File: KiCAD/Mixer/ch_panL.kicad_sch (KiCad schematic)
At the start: 8 parts, among them J4 Conn_01x02_Socket, J5 Conn_01x02_Socket, U1 NE5532

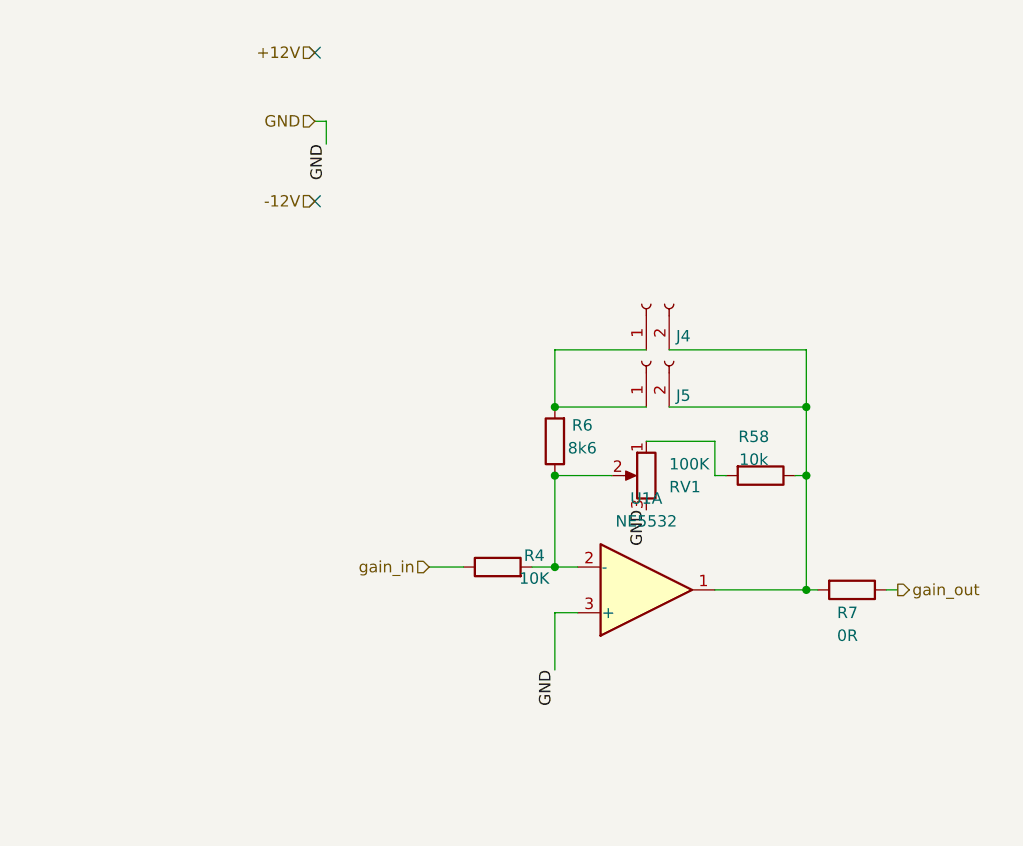
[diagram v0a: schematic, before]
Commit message: Rework of schematic, with error fixes and reworked pcb
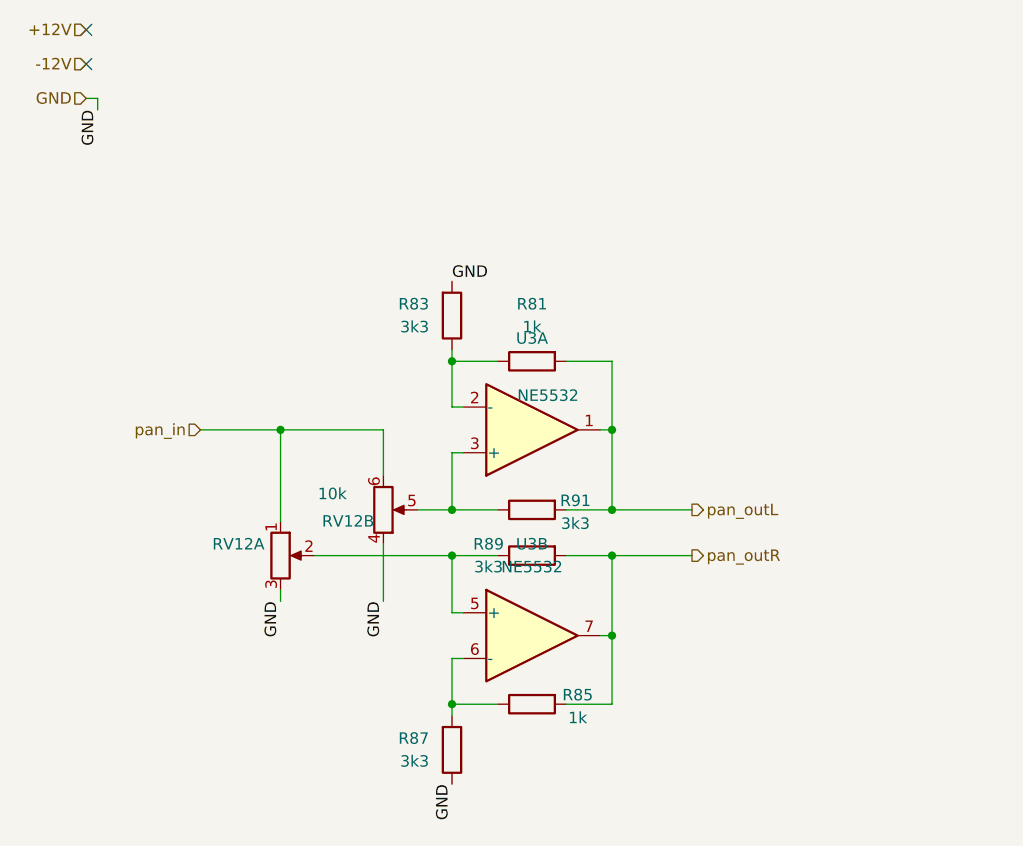
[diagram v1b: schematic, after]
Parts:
- removed J4, J5: Conn_01x02_Socket, Connector_PinSocket_2.54mm:PinSocket_1x02_P2.54mm_Vertical, symbol Connector:Conn_01x02_Socket
- removed R4: 10K, Resistor_SMD:R_0805_2012Metric_Pad1.20x1.40mm_HandSolder, symbol Device:R
- removed R58: 10k, Resistor_SMD:R_0805_2012Metric_Pad1.20x1.40mm_HandSolder, symbol Device:R
- removed R6: 8k6, Resistor_SMD:R_0805_2012Metric_Pad1.20x1.40mm_HandSolder, symbol Device:R
- removed R7: 0R, Resistor_SMD:R_0805_2012Metric_Pad1.20x1.40mm_HandSolder, symbol Device:R
- removed RV1: 100K, Potentiometer_THT:Potentiometer_Alps_RK09K_Single_Vertical, symbol Device:R_Potentiometer
- removed U1: NE5532, Package_SO:SOIC-8_3.9x4.9mm_P1.27mm, symbol Amplifier_Operational:NE5532
- added R81, R85: 1k, Resistor_SMD:R_0805_2012Metric_Pad1.20x1.40mm_HandSolder, symbol Device:R
- added R83, R87, R89, R91: 3k3, Resistor_SMD:R_0805_2012Metric_Pad1.20x1.40mm_HandSolder, symbol Device:R
- added RV12: 10k, Potentiometer_THT:Potentiometer_Alps_RK09L_Double_Vertical, symbol Device:R_Potentiometer_Dual_Separate
- added U3: NE5532, Package_SO:SOIC-8_3.9x4.9mm_P1.27mm, symbol Amplifier_Operational:NE5532
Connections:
- net GND: now also R83.2, R87.1, RV12.3, RV12.4
- new net: R89.1, RV12.2, U3.5 (+)
- new net: R81.1, R83.1, U3.2 (-)
- new net: R91.1, RV12.5, U3.3 (+)
- new net: R85.1, R87.2, U3.6 (-)
- new net pan_in: RV12.1, RV12.6
- new net pan_outL: R81.2, R91.2, U3.1
- new net pan_outR: R85.2, R89.2, U3.7

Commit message: Final PCB Version that got ordered from JLCPCB
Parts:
- removed R81, R85: 1k, Resistor_SMD:R_0805_2012Metric_Pad1.20x1.40mm_HandSolder, symbol Device:R
- removed R83, R87, R89, R91: 3k3, Resistor_SMD:R_0805_2012Metric_Pad1.20x1.40mm_HandSolder, symbol Device:R
- removed RV12: 10k, Potentiometer_THT:Potentiometer_Alps_RK09L_Double_Vertical, symbol Device:R_Potentiometer_Dual_Separate
- added R69, R70, R72, R73: 3k3, Resistor_SMD:R_0805_2012Metric_Pad1.20x1.40mm_HandSolder, symbol Device:R
- added R71, R74: 1k, Resistor_SMD:R_0805_2012Metric_Pad1.20x1.40mm_HandSolder, symbol Device:R
- added RV10: 10k, Potentiometer_THT:Potentiometer_Alps_RK09L_Double_Vertical, symbol Device:R_Potentiometer_Dual_Separate
- renumbered U3 to U10
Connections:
- net GND: now also R69.2, R70.1, RV10.3, RV10.4
- net pan_in: now also RV10.1, RV10.6
- net pan_outL: now also R71.2, R72.2
- net pan_outR: now also R73.2, R74.2
- net at U10.5 (+): now also R73.1, RV10.2
- net at U10.2 (-): now also R69.1, R71.1
- net at U10.3 (+): now also R72.1, RV10.5
- net at U10.6 (-): now also R70.2, R74.1
